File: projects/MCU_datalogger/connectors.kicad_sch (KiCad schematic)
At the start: 4 parts, among them J1 Conn_01x04_Pin, J2 Conn_01x04_Pin, J3 Conn_02x03_Odd_Even, J4 Conn_01x09_Pin

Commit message: MC_datalogger - Arrange and anotate symbols
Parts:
- renumbered J4 to J2, J2 to J3, J3 to J4
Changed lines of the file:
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@@
+				)
+			)
+			(project "connectors"
+				(path "/9dc420f9-f07a-45e1-a4a3-05f19fbf9e8e"
+					(reference "J1")
+					(unit 1)
 				)
 			)
@@
 		(on_board yes)
 		(dnp no)
-		(property "Reference" "J3"
+		(property "Reference" "J4"
 			(at 179.07 110.49 0)
 			(effects
@@
 			(project ""
 				(path "/7bf4f70a-c379-4f6a-bba1-afc53ccea3c5/f748de0e-ad40-4233-8c36-6ac943b70eee"
-					(reference "J3")
+					(reference "J4")
+					(unit 1)
+				)
+			)
+			(project "connectors"
+				(path "/9dc420f9-f07a-45e1-a4a3-05f19fbf9e8e"
+					(reference "J4")
 					(unit 1)
 				)
@@
 		(on_board yes)
 		(dnp no)
-		(property "Reference" "J4"
+		(property "Reference" "J2"
 			(at 99.06 110.49 0)
 			(effects
@@
 			(project ""
 				(path "/7bf4f70a-c379-4f6a-bba1-afc53ccea3c5/f748de0e-ad40-4233-8c36-6ac943b70eee"
-					(reference "J4")
+					(reference "J2")
+					(unit 1)
+				)
+			)
+			(project "connectors"
+				(path "/9dc420f9-f07a-45e1-a4a3-05f19fbf9e8e"
+					(reference "J2")
 					(unit 1)
 				)
@@
 		(on_board yes)
 		(dnp no)
-		(property "Reference" "J2"
+		(property "Reference" "J3"
 			(at 179.07 69.85 0)
 			(effects
@@
 			(project "MCU_datalogger"
 				(path "/7bf4f70a-c379-4f6a-bba1-afc53ccea3c5/f748de0e-ad40-4233-8c36-6ac943b70eee"
-					(reference "J2")
-					(unit 1)
-				)
-			)
-		)
-	)
+					(reference "J3")
+					(unit 1)
+				)
+			)
+			(project "connectors"
+				(path "/9dc420f9-f07a-45e1-a4a3-05f19fbf9e8e"
+					(reference "J3")
+					(unit 1)
+				)
+			)
+		)
+	)
+	(sheet_instances
+		(path "/"
+			(page "1")
+		)
+	)
+	(embedded_fonts no)
 )

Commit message: MCU datalogger - associate footprints
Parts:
- J1, J3: footprint (none) -> Connector_PinHeader_2.54mm:PinHeader_1x04_P2.54mm_Vertical
- J2: footprint (none) -> Connector_PinHeader_2.54mm:PinHeader_1x09_P2.54mm_Vertical
- J4: footprint (none) -> Connector_PinHeader_2.54mm:PinHeader_2x03_P2.54mm_Vertical
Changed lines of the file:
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@@
 			)
 		)
-		(property "Footprint" ""
+		(property "Footprint" "Connector_PinHeader_2.54mm:PinHeader_1x04_P2.54mm_Vertical"
 			(at 96.52 78.74 0)
 			(effects
@@
 			)
 		)
-		(property "Footprint" ""
+		(property "Footprint" "Connector_PinHeader_2.54mm:PinHeader_2x03_P2.54mm_Vertical"
 			(at 177.8 119.38 0)
 			(effects
@@
 			)
 		)
-		(property "Footprint" ""
+		(property "Footprint" "Connector_PinHeader_2.54mm:PinHeader_1x09_P2.54mm_Vertical"
 			(at 96.52 127 0)
 			(effects
@@
 			)
 		)
-		(property "Footprint" ""
+		(property "Footprint" "Connector_PinHeader_2.54mm:PinHeader_1x04_P2.54mm_Vertical"
 			(at 176.53 78.74 0)
 			(effects

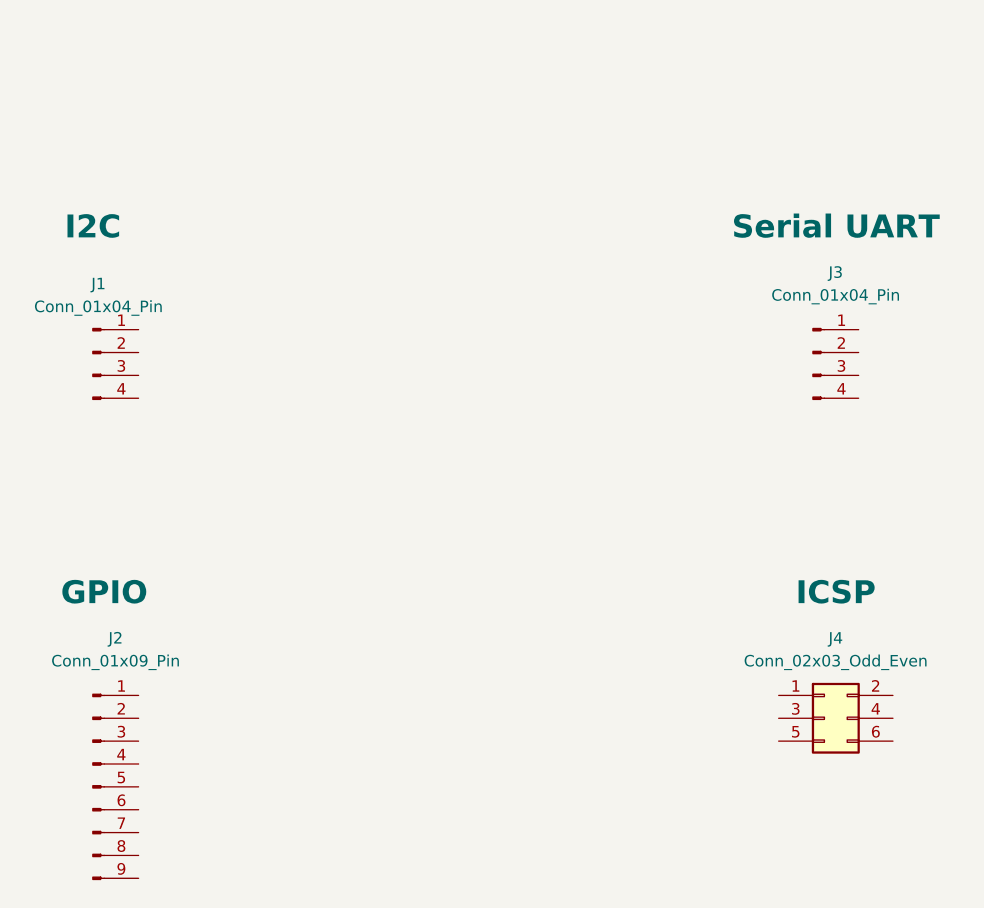
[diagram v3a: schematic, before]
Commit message: MCU datalogger - wiring of second sheet
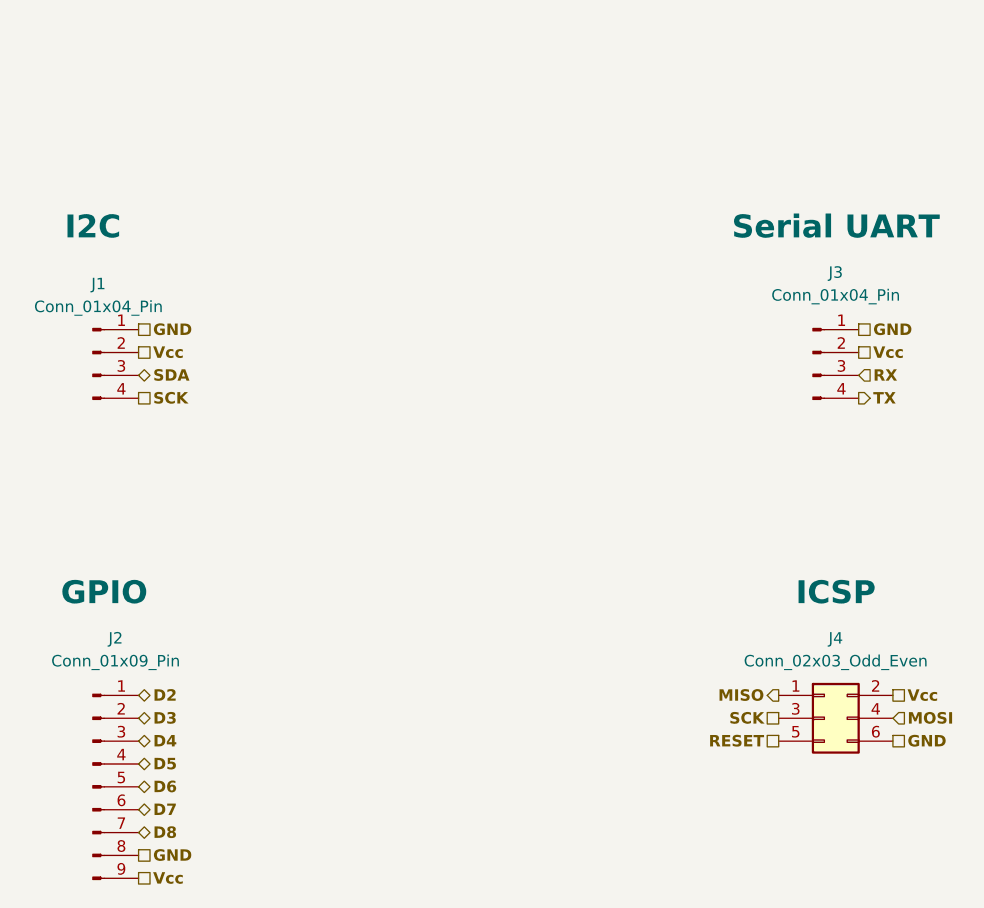
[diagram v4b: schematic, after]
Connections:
- net GND: now reaches J1.1 (Pin_1)
- net GND: now also J2.8 (Pin_8), J3.1 (Pin_1), J4.6 (Pin_6)
- net Vcc: now reaches J1.2 (Pin_2)
- net Vcc: now also J2.9 (Pin_9), J3.2 (Pin_2), J4.2 (Pin_2)
- net SDA: now reaches J1.3 (Pin_3)
- net SCK: now reaches J1.4 (Pin_4)
- net SCK: now also J4.3 (Pin_3)
- net MISO: now reaches J4.1 (Pin_1)
- net MOSI: now reaches J4.4 (Pin_4)
- net RESET: now reaches J4.5 (Pin_5)
- net D2: now reaches J2.1 (Pin_1)
- net D3: now reaches J2.2 (Pin_2)
- net D4: now reaches J2.3 (Pin_3)
- net D5: now reaches J2.4 (Pin_4)
- net D6: now reaches J2.5 (Pin_5)
- net D7: now reaches J2.6 (Pin_6)
- net D8: now reaches J2.7 (Pin_7)
- net RX: now reaches J3.3 (Pin_3)
- net TX: now reaches J3.4 (Pin_4)

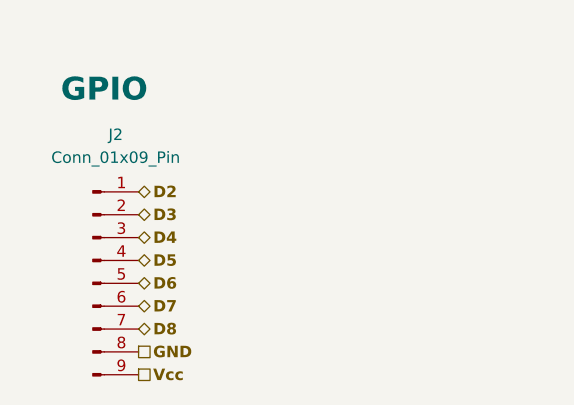
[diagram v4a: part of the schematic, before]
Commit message: MCU datalogger v1.2
- fix missing Vcc label in Battery + net
- fix the resulting violations of Vcc routing (wider tracks required)
- reorder pins of GPIO connector to make Pin 1 is GND
- Add silkscreen labels to connectors I2C ICSP Serial and GPIO
- other minor adjustments to component placements and silkscreen
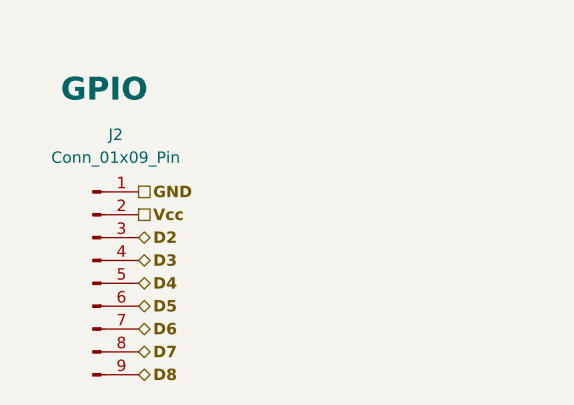
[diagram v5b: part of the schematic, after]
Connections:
- net D2: now also J2.3 (Pin_3); no longer J2.1 (Pin_1)
- net D3: now also J2.4 (Pin_4); no longer J2.2 (Pin_2)
- net D4: now also J2.5 (Pin_5); no longer J2.3 (Pin_3)
- net D5: now also J2.6 (Pin_6); no longer J2.4 (Pin_4)
- net D6: now also J2.7 (Pin_7); no longer J2.5 (Pin_5)
- net D7: now also J2.8 (Pin_8); no longer J2.6 (Pin_6)
- net D8: now also J2.9 (Pin_9); no longer J2.7 (Pin_7)
- net GND: now also J2.1 (Pin_1); no longer J2.8 (Pin_8)
- net Vcc: now also J2.2 (Pin_2); no longer J2.9 (Pin_9)
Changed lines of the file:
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@@
 		(comment 3 "KiCAD like a Pro - Udemy Course (Project 4)")
 	)
+	(hierarchical_label "SDA"
+		(shape bidirectional)
+		(at 101.6 81.28 0)
+		(effects
+			(font
+				(size 1.27 1.27)
+				(thickness 0.254)
+				(bold yes)
+			)
+			(justify left)
+		)
+	)
+	(hierarchical_label "D3"
+		(shape bidirectional)
+		(at 101.6 124.46 0)
+		(effects
+			(font
+				(size 1.27 1.27)
+				(thickness 0.254)
+				(bold yes)
+			)
+			(justify left)
+		)
+	)
+	(hierarchical_label "D7"
+		(shape bidirectional)
+		(at 101.6 134.62 0)
+		(effects
+			(font
+				(size 1.27 1.27)
+				(thickness 0.254)
+				(bold yes)
+			)
+			(justify left)
+		)
+	)
+	(hierarchical_label "Vcc"
+		(shape passive)
+		(at 185.42 116.84 0)
+		(effects
+			(font
+				(size 1.27 1.27)
+				(thickness 0.254)
+				(bold yes)
+			)
+			(justify left)
+		)
+	)
+	(hierarchical_label "RESET"
+		(shape passive)
+		(at 172.72 121.92 180)
+		(effects
+			(font
+				(size 1.27 1.27)
+				(thickness 0.254)
+				(bold yes)
+			)
+			(justify right)
+		)
+	)
+	(hierarchical_label "Vcc"
+		(shape passive)
+		(at 181.61 78.74 0)
+		(effects
+			(font
+				(size 1.27 1.27)
+				(thickness 0.254)
+				(bold yes)
+			)
+			(justify left)
+		)
+	)
+	(hierarchical_label "Vcc"
+		(shape passive)
+		(at 101.6 119.38 0)
+		(effects
+			(font
+				(size 1.27 1.27)
+				(thickness 0.254)
+				(bold yes)
+			)
+			(justify left)
+		)
+	)
+	(hierarchical_label "D4"
+		(shape bidirectional)
+		(at 101.6 127 0)
+		(effects
+			(font
+				(size 1.27 1.27)
+				(thickness 0.254)
+				(bold yes)
+			)
+			(justify left)
+		)
+	)
+	(hierarchical_label "GND"
+		(shape passive)
+		(at 181.61 76.2 0)
+		(effects
+			(font
+				(size 1.27 1.27)
+				(thickness 0.254)
+				(bold yes)
+			)
+			(justify left)
+		)
+	)
+	(hierarchical_label "SCK"
+		(shape passive)
+		(at 101.6 83.82 0)
+		(effects
+			(font
+				(size 1.27 1.27)
+				(thickness 0.254)
+				(bold yes)
+			)
+			(justify left)
+		)
+	)
+	(hierarchical_label "GND"
+		(shape passive)
+		(at 101.6 76.2 0)
+		(effects
+			(font
+				(size 1.27 1.27)
+				(thickness 0.254)
+				(bold yes)
+			)
+			(justify left)
+		)
+	)
 	(hierarchical_label "D6"
 		(shape bidirectional)
-		(at 101.6 127 0)
-		(effects
-			(font
-				(size 1.27 1.27)
-				(thickness 0.254)
-				(bold yes)
-			)
-			(justify left)
-		)
-	)
-	(hierarchical_label "SDA"
-		(shape bidirectional)
-		(at 101.6 81.28 0)
-		(effects
-			(font
-				(size 1.27 1.27)
-				(thickness 0.254)
-				(bold yes)
-			)
-			(justify left)
-		)
-	)
-	(hierarchical_label "D2"
-		(shape bidirectional)
-		(at 101.6 116.84 0)
-		(effects
-			(font
-				(size 1.27 1.27)
-				(thickness 0.254)
-				(bold yes)
-			)
-			(justify left)
-		)
-	)
-	(hierarchical_label "Vcc"
-		(shape passive)
-		(at 185.42 116.84 0)
-		(effects
-			(font
-				(size 1.27 1.27)
-				(thickness 0.254)
-				(bold yes)
-			)
-			(justify left)
-		)
-	)
-	(hierarchical_label "RESET"
-		(shape passive)
-		(at 172.72 121.92 180)
-		(effects
-			(font
-				(size 1.27 1.27)
-				(thickness 0.254)
-				(bold yes)
-			)
-			(justify right)
-		)
-	)
-	(hierarchical_label "Vcc"
-		(shape passive)
+		(at 101.6 132.08 0)
+		(effects
+			(font
+				(size 1.27 1.27)
+				(thickness 0.254)
+				(bold yes)
+			)
+			(justify left)
+		)
+	)
+	(hierarchical_label "D8"
+		(shape bidirectional)
 		(at 101.6 137.16 0)
-		(effects
-			(font
-				(size 1.27 1.27)
-				(thickness 0.254)
-				(bold yes)
-			)
-			(justify left)
-		)
-	)
-	(hierarchical_label "Vcc"
-		(shape passive)
-		(at 181.61 78.74 0)
-		(effects
-			(font
-				(size 1.27 1.27)
-				(thickness 0.254)
-				(bold yes)
-			)
-			(justify left)
-		)
-	)
-	(hierarchical_label "D3"
-		(shape bidirectional)
-		(at 101.6 119.38 0)
-		(effects
-			(font
-				(size 1.27 1.27)
-				(thickness 0.254)
-				(bold yes)
-			)
-			(justify left)
-		)
-	)
-	(hierarchical_label "D8"
-		(shape bidirectional)
-		(at 101.6 132.08 0)
-		(effects
-			(font
-				(size 1.27 1.27)
-				(thickness 0.254)
-				(bold yes)
-			)
-			(justify left)
-		)
-	)
-	(hierarchical_label "D7"
-		(shape bidirectional)
-		(at 101.6 129.54 0)
-		(effects
-			(font
-				(size 1.27 1.27)
-				(thickness 0.254)
-				(bold yes)
-			)
-			(justify left)
-		)
-	)
-	(hierarchical_label "GND"
-		(shape passive)
-		(at 181.61 76.2 0)
-		(effects
-			(font
-				(size 1.27 1.27)
-				(thickness 0.254)
-				(bold yes)
-			)
-			(justify left)
-		)
-	)
-	(hierarchical_label "SCK"
-		(shape passive)
-		(at 101.6 83.82 0)
-		(effects
-			(font
-				(size 1.27 1.27)
-				(thickness 0.254)
-				(bold yes)
-			)
-			(justify left)
-		)
-	)
-	(hierarchical_label "GND"
-		(shape passive)
-		(at 101.6 76.2 0)
-		(effects
-			(font
-				(size 1.27 1.27)
-				(thickness 0.254)
-				(bold yes)
-			)
-			(justify left)
-		)
-	)
-	(hierarchical_label "D5"
-		(shape bidirectional)
-		(at 101.6 124.46 0)
-		(effects
-			(font
-				(size 1.27 1.27)
-				(thickness 0.254)
-				(bold yes)
-			)
-			(justify left)
-		)
-	)
-	(hierarchical_label "GND"
-		(shape passive)
-		(at 101.6 134.62 0)
 		(effects
 			(font
@@
 		)
 	)
-	(hierarchical_label "D4"
-		(shape bidirectional)
-		(at 101.6 121.92 0)
-		(effects
-			(font
-				(size 1.27 1.27)
-				(thickness 0.254)
-				(bold yes)
-			)
-			(justify left)
-		)
-	)
 	(hierarchical_label "MOSI"
 		(shape input)
@@
 		)
 	)
+	(hierarchical_label "D5"
+		(shape bidirectional)
+		(at 101.6 129.54 0)
+		(effects
+			(font
+				(size 1.27 1.27)
+				(thickness 0.254)
+				(bold yes)
+			)
+			(justify left)
+		)
+	)
 	(hierarchical_label "GND"
 		(shape passive)
@@
 		)
 	)
+	(hierarchical_label "GND"
+		(shape passive)
+		(at 101.6 116.84 0)
+		(effects
+			(font
+				(size 1.27 1.27)
+				(thickness 0.254)
+				(bold yes)
+			)
+			(justify left)
+		)
+	)
+	(hierarchical_label "D2"
+		(shape bidirectional)
+		(at 101.6 121.92 0)
+		(effects
+			(font
+				(size 1.27 1.27)
+				(thickness 0.254)
+				(bold yes)
+			)
+			(justify left)
+		)
+	)

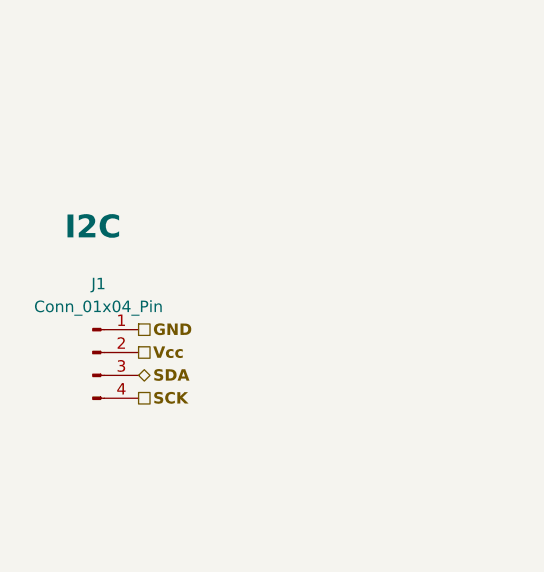
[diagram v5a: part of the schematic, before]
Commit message: MCU datalogger schematic - fix bug in SCL and SCK clock signals
Rename SCK net label to SCL where appropriate in both schematic
drawings (Root and Connectors) to fix bug where pins 17 and 28
of the ATMEGA were incorrectly shorted because of a confusion of
two clock different signals:
- SCK for ICSP
- SCL for I2C
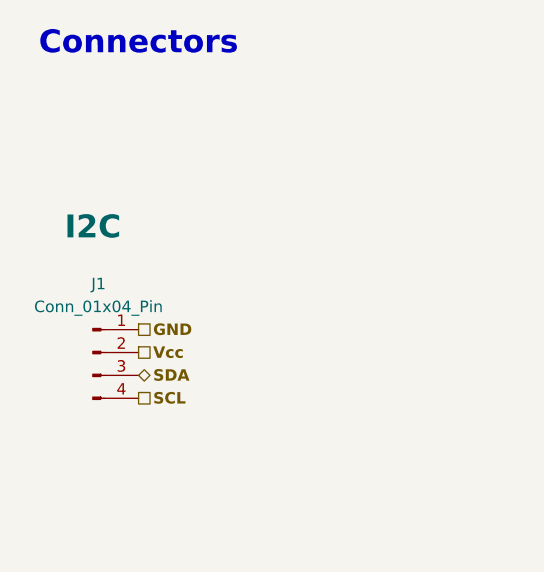
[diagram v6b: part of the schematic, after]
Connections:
- net SCK: no longer J1.4 (Pin_4)
- new net SCL: J1.4 (Pin_4)
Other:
- note added: "Connectors"
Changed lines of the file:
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@@
 		(comment 3 "KiCAD like a Pro - Udemy Course (Project 4)")
+	)
+	(text "Connectors"
+		(exclude_from_sim no)
+		(at 101.6 44.45 0)
+		(effects
+			(font
+				(size 2.54 2.54)
+				(thickness 0.508)
+				(bold yes)
+			)
+		)
 	)
 	(hierarchical_label "SDA"
@@
 		)
 	)
-	(hierarchical_label "SCK"
+	(hierarchical_label "SCL"
 		(shape passive)
 		(at 101.6 83.82 0)

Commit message: MCU datalogger - add BOM, modify polarized cap, add datasheets
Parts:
- J1, J2, J3, J4: LCSC# (none) -> stash
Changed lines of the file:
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@@
 	(title_block
 		(title "MCU datalogger")
-		(date "2025-12-24")
-		(rev "0.1")
+		(date "2026-03-18")
+		(rev "0.2")
 		(company "Manuel Heredia - sevillabot")
 		(comment 1 "--")
@@
 			)
 		)
+		(property "LCSC#" "stash"
+			(at 96.52 78.74 0)
+			(effects
+				(font
+					(size 1.27 1.27)
+				)
+				(hide yes)
+			)
+		)
 		(pin "4"
 		)
@@
 			)
 		)
+		(property "LCSC#" "stash"
+			(at 177.8 119.38 0)
+			(effects
+				(font
+					(size 1.27 1.27)
+				)
+				(hide yes)
+			)
+		)
 		(pin "5"
 		)
@@
 			)
 		)
+		(property "LCSC#" "stash"
+			(at 96.52 127 0)
+			(effects
+				(font
+					(size 1.27 1.27)
+				)
+				(hide yes)
+			)
+		)
 		(pin "7"
 		)
@@
 			(at 176.53 78.74 0)
 			(effects
+				(font
+					(size 1.27 1.27)
+				)
+				(hide yes)
+			)
+		)
+		(property "LCSC#" "stash"
+			(at 176.53 78.74 0)
+			(effects
